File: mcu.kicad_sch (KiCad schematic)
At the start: 18 parts, among them CN1 FTSH-107-01-L-DV-K, U1 STM32H743VITx

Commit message: corrections and IO updated
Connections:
- net FDCAN1_RX: now also U1.81 (PD0); no longer U1.82 (PD1)
- net FDCAN1_TX: now also U1.82 (PD1); no longer U1.81 (PD0)
- net I2C3_SCL: no longer U1.67 (PA8)
- net I2C3_SDA: no longer U1.66 (PC9)
- net SWCLK: now also U1.76 (PA14); no longer U1.72 (PA13)
- net SWDIO: now also U1.72 (PA13); no longer U1.76 (PA14)
- net UART4_RX: now also U1.95 (PB8); no longer U1.96 (PB9)
- net UART4_TX: now also U1.96 (PB9); no longer U1.95 (PB8)
- net USART3_RX: now also U1.56 (PD9); no longer U1.79 (PC11)
- net USART3_TX: now also U1.55 (PD8); no longer U1.78 (PC10)
- net I2C4_SCL: now reaches U1.59 (PD12)
- net I2C4_SDA: now reaches U1.60 (PD13)
- net D0: now reaches U1.65 (PC8)
- net CK: now reaches U1.80 (PC12)
- net CMD: now reaches U1.83 (PD2)
- new net D1: U1.66 (PC9)
- new net D2: U1.78 (PC10)
- new net D3: U1.79 (PC11)

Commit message: mcu updates
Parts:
- added C19, C9: 2.2uF, Capacitor_SMD:C_0201_0603Metric_Pad0.64x0.40mm_HandSolder, symbol Device:C_Small
- added C33, C40: 100nF, Capacitor_SMD:C_0201_0603Metric_Pad0.64x0.40mm_HandSolder, symbol Device:C_Small
- added C39, C41: 1uF, Capacitor_SMD:C_0201_0603Metric_Pad0.64x0.40mm_HandSolder, symbol Device:C_Small
- added JP1: Jumper_2_Bridged, symbol Jumper:Jumper_2_Bridged
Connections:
- net I2C3_SCL is gone; now on net I2C4_SCL: R13.2
- net I2C3_SDA is gone; now on net I2C4_SDA: R14.2
- net +3V3: now also JP1.1 (A); no longer C7.1, CN1.12, U1.14 (NRST)
- net BOOT0: now also JP1.2 (B)
- net GND: now also C19.1, C33.2, C39.2, C40.2, C41.2, C9.2
- net C8Mhz_1: now reaches U1.12 (PH0)
- net C8Mhz_2: now reaches U1.13 (PH1)
- net TIM1_CH1: now reaches U1.39 (PE9)
- net TIM1_CH2: now reaches U1.41 (PE11)
- net TIM1_CH3: now reaches U1.43 (PE13)
- net TIM1_CH4: now reaches U1.44 (PE14)
- net at U1.48 (VCAP): now also C9.1
- net at U1.73 (VCAP): now also C19.2
- net +3.3VA renamed +3.3A
- net +3.3A: now also C33.1, C39.1, C40.1, C41.1
- new net NRST: C7.1, CN1.12, U1.14 (NRST)
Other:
- moved on the sheet: C7, R1

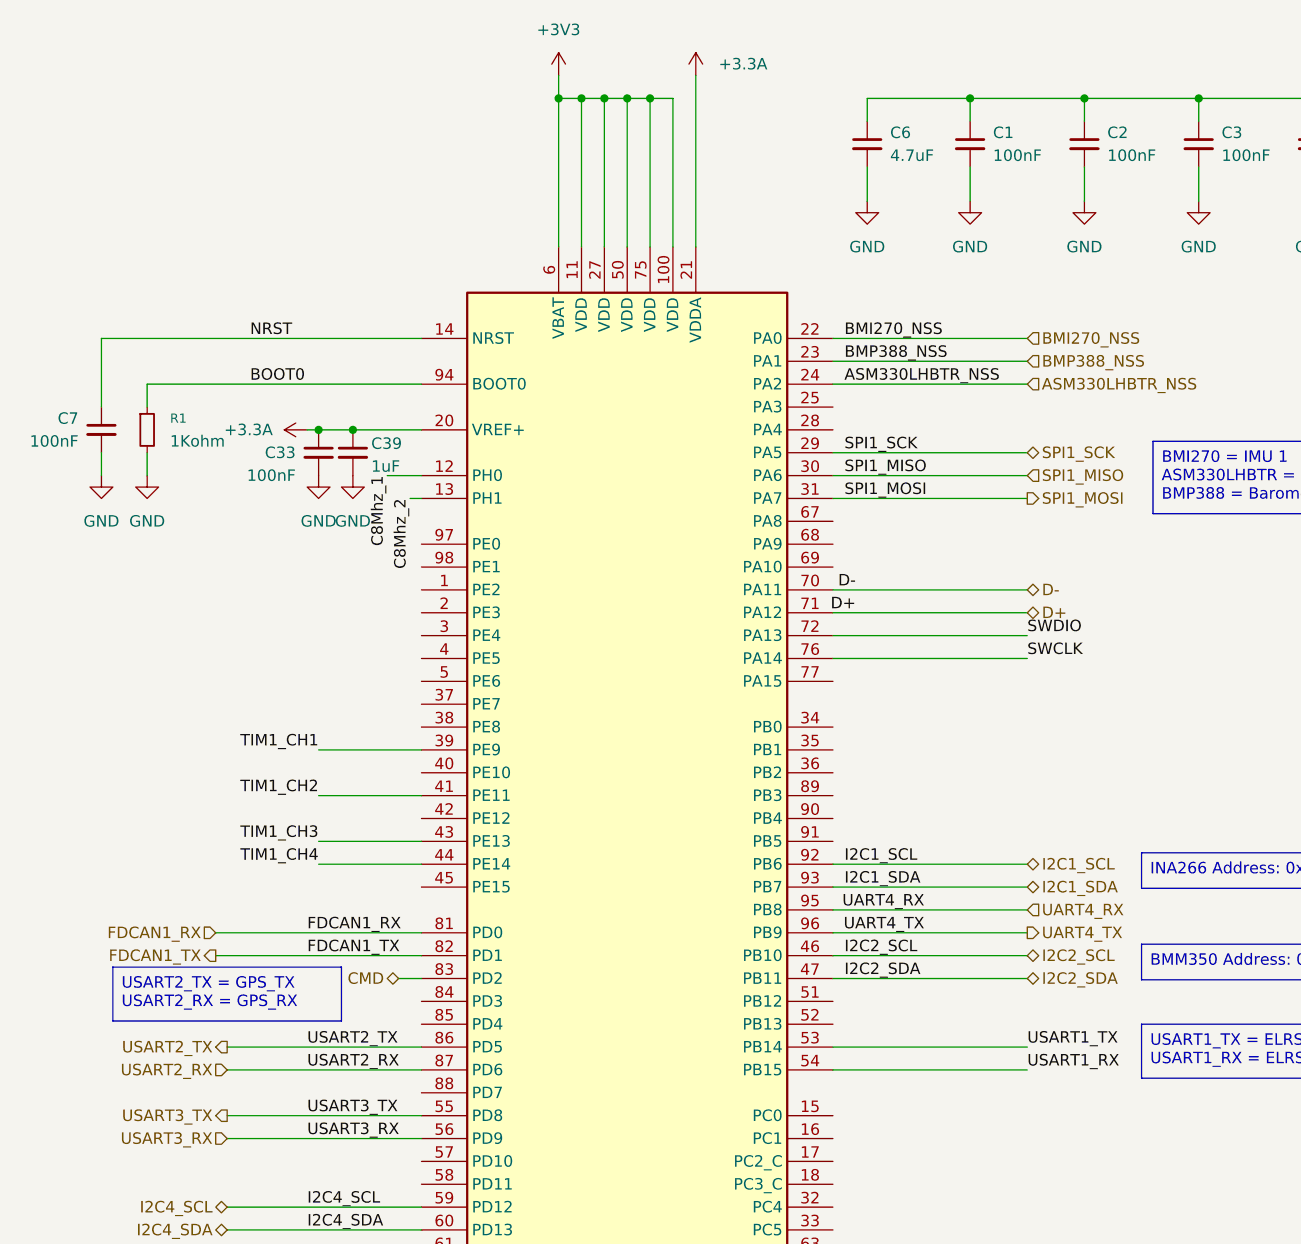
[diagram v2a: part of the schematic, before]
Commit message: added in RF componentys and updated and reviewed STM connections
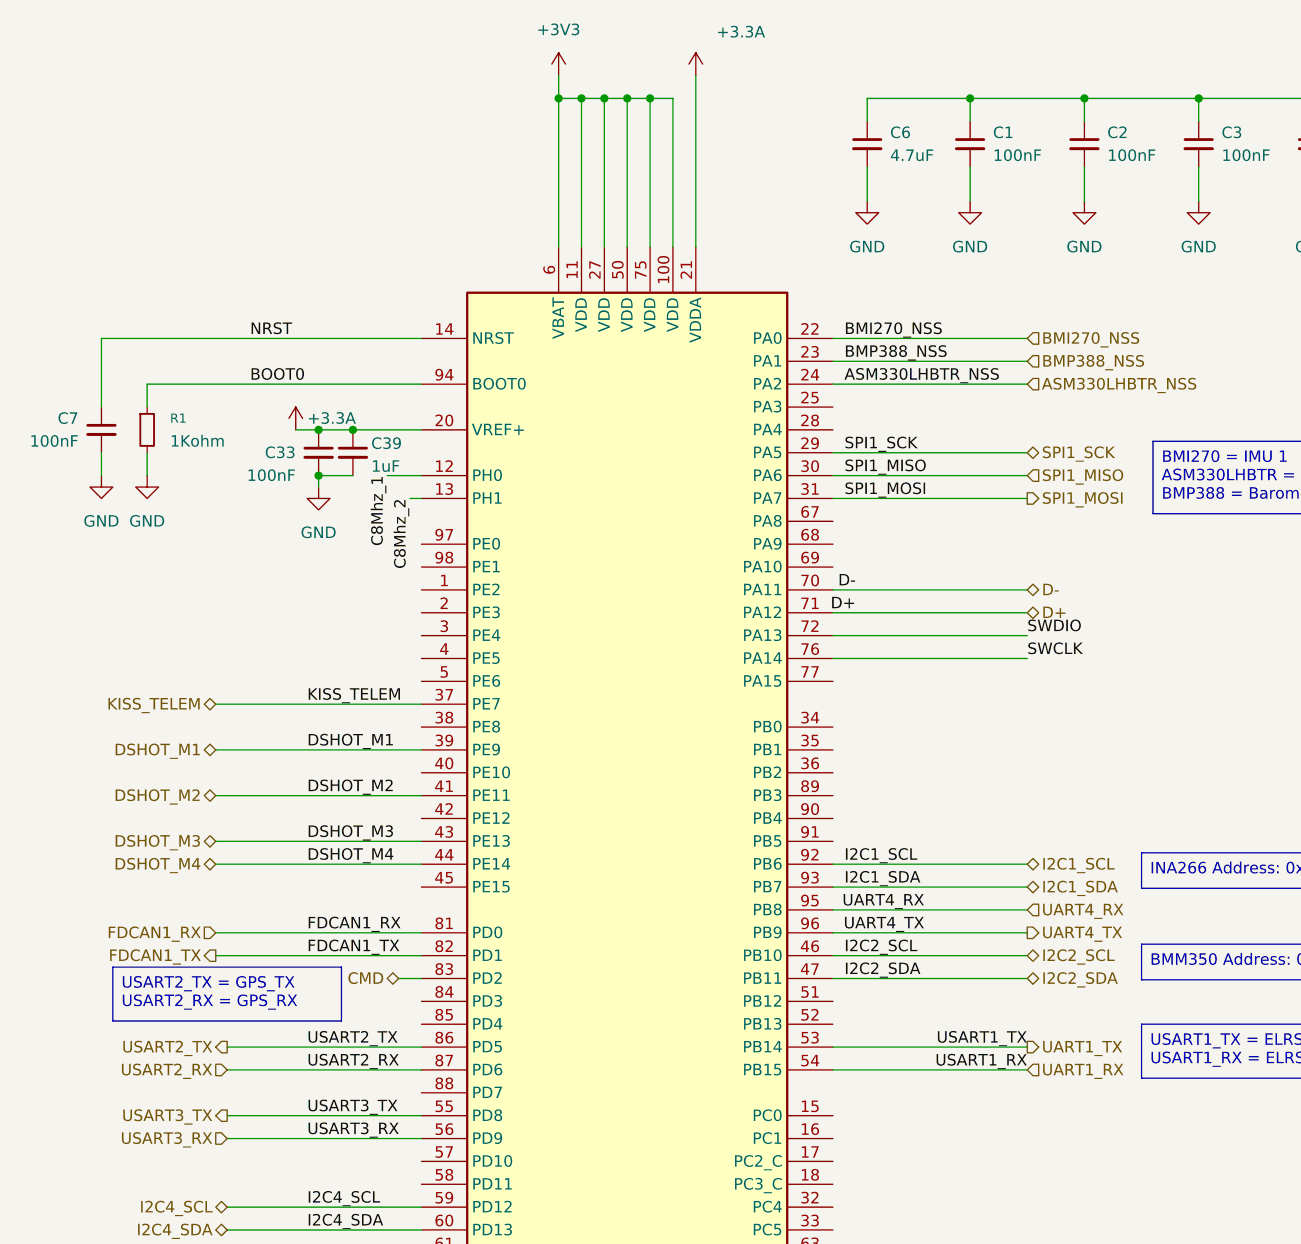
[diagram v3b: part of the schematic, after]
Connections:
- net KISS_TELEM: now reaches U1.37 (PE7)
- net TIM1_CH1 renamed DSHOT_M1
- net TIM1_CH2 renamed DSHOT_M2
- net TIM1_CH3 renamed DSHOT_M3
- net TIM1_CH4 renamed DSHOT_M4
- net USART1_RX renamed UART1_RX
- net USART1_TX renamed UART1_TX

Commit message: finalized RF
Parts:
- added JP5: Jumper_2_Open, symbol Jumper:Jumper_2_Open
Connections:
- net GND: now also JP5.1 (A)
- net NRST: now also JP5.2 (B)
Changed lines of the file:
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@@
 	)
 	(junction
+		(at 21.59 50.8)
+		(diameter 0)
+		(color 0 0 0 0)
+	)
+	(junction
 		(at 130.81 24.13)
 		(diameter 0)
@@
 	(wire
 		(pts
+			(xy 16.51 40.64) (xy 21.59 40.64)
+		)
+		(stroke
+			(width 0)
+			(type default)
+		)
+	)
+	(wire
+		(pts
 			(xy 34.29 116.84) (xy 57.15 116.84)
 		)
@@
 	)
 	(symbol
+		(lib_id "Jumper:Jumper_2_Open")
+		(at 21.59 45.72 270)
+		(unit 1)
+		(body_style 1)
+		(exclude_from_sim no)
+		(in_bom yes)
+		(on_board yes)
+		(in_pos_files yes)
+		(dnp no)
+		(fields_autoplaced yes)
+		(property "Reference" "JP5"
+			(at 24.13 44.4499 90)
+			(show_name no)
+			(do_not_autoplace no)
+			(effects
+				(font
+					(size 1.27 1.27)
+				)
+				(justify left)
+			)
+		)
+		(property "Value" "Jumper_2_Open"
+			(at 24.13 46.9899 90)
+			(show_name no)
+			(do_not_autoplace no)
+			(effects
+				(font
+					(size 1.27 1.27)
+				)
+				(justify left)
+			)
+		)
+		(property "Footprint" ""
+			(at 21.59 45.72 0)
+			(hide yes)
+			(show_name no)
+			(do_not_autoplace no)
+			(effects
+				(font
+					(size 1.27 1.27)
+				)
+			)
+		)
+		(property "Datasheet" ""
+			(at 21.59 45.72 0)
+			(hide yes)
+			(show_name no)
+			(do_not_autoplace no)
+			(effects
+				(font
+					(size 1.27 1.27)
+				)
+			)
+		)
+		(property "Description" "Jumper, 2-pole, open"
+			(at 21.59 45.72 0)
+			(hide yes)
+			(show_name no)
+			(do_not_autoplace no)
+			(effects
+				(font
+					(size 1.27 1.27)
+				)
+			)
+		)
+		(pin "2"
+		)
+		(pin "1"
+		)
+		(instances
+			(project "FlightComputer"
+				(path "/c0a97758-75a3-49d0-abcc-edce55d99095/57068174-e220-4e49-a97a-8507f2dd583c"
+					(reference "JP5")
+					(unit 1)
+				)
+			)
+		)
+	)
+	(symbol
 		(lib_id "power:GND")
 		(at 130.81 35.56 0)
@@
 					(unit 1)
 				)
+			)
+		)
+	)
+	(symbol
+		(lib_id "power:GND")
+		(at 16.51 40.64 0)
+		(unit 1)
+		(body_style 1)
+		(exclude_from_sim no)
+		(in_bom yes)
+		(on_board yes)
+		(in_pos_files yes)
+		(dnp no)
+		(fields_autoplaced yes)
+		(property "Reference" "#PWR0148"
+			(at 16.51 46.99 0)
+			(hide yes)
+			(show_name no)
+			(do_not_autoplace no)
+			(effects
+				(font
+					(size 1.27 1.27)
+				)
+			)
+		)
+		(property "Value" "GND"
+			(at 16.51 45.72 0)
+			(show_name no)
+			(do_not_autoplace no)
+			(effects
+				(font
+					(size 1.27 1.27)
+				)
+			)
+		)
+		(property "Footprint" ""
+			(at 16.51 40.64 0)
+			(hide yes)
+			(show_name no)
+			(do_not_autoplace no)
+			(effects
+				(font
+					(size 1.27 1.27)
+				)
+			)
+		)
+		(property "Datasheet" ""
+			(at 16.51 40.64 0)
+			(hide yes)
+			(show_name no)
+			(do_not_autoplace no)
+			(effects
+				(font
+					(size 1.27 1.27)
+				)
+			)
+		)
+		(property "Description" "Power symbol creates a global label with name \"GND\" , ground"
+			(at 16.51 40.64 0)
+			(hide yes)
+			(show_name no)
+			(do_not_autoplace no)
+			(effects
+				(font
+					(size 1.27 1.27)
+				)
+			)
+		)
+		(pin "1"
+		)
+		(instances
+			(project "FlightComputer"
+				(path "/c0a97758-75a3-49d0-abcc-edce55d99095/57068174-e220-4e49-a97a-8507f2dd583c"
+					(reference "#PWR0148")
+					(unit 1)
+				)
